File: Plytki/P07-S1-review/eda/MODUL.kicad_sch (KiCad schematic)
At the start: 23 parts, among them J5 J_MOD, U16 74AHCT125D, U17 74LVC2G17

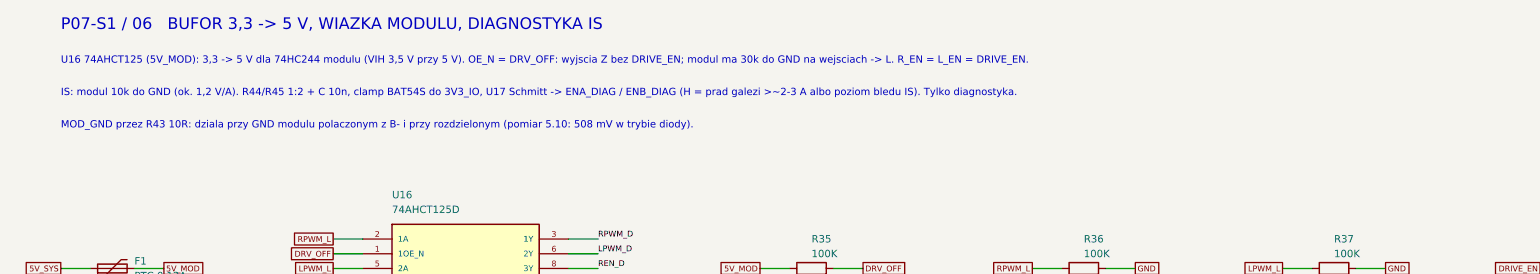
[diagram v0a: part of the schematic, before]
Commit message: P07 S1: decyzje użytkownika 5.10 w schemacie — KPWR G2RL-1-E DC5 z 5V_SYS (Q1 AO3400A, clamp do 5V_SYS, C9), J5 IDC 2x4 1:1 i wiązka W5 w BOM, F1 7,5 A, ENA/ENB_DIAG; kontrole 16/16 (mutacje 22/22), S1 30/30
Co-Authored-By: Claude Opus 5.5 <noreply@anthropic.com>
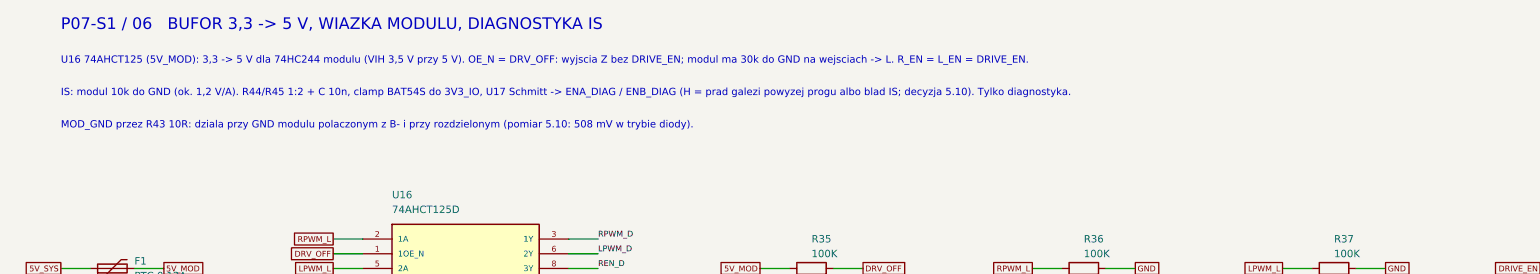
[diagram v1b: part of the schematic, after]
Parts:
- J5: MPN IDC header 2x4 2.54 mm angled shrouded, Au -> IDC box header 2x4 2.54 mm angled shrouded, Au
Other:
- note added: "IS: modul 10k do GND (ok. 1,2 V/A). R44/R45 1:2 + C 10n, clamp BAT54S do 3V3_IO, U17 Schmitt -> ENA_DIAG / ENB_DIAG (H = prad galezi powyzej progu albo blad IS; decyzja 5.10). Tylko diagnostyka."
- note removed: "IS: modul 10k do GND (ok. 1,2 V/A). R44/R45 1:2 + C 10n, clamp BAT54S do 3V3_IO, U17 Schmitt -> ENA_DIAG / ENB_DIAG (H = prad galezi >~2-3 A albo poziom bledu IS). Tylko diagnostyka."

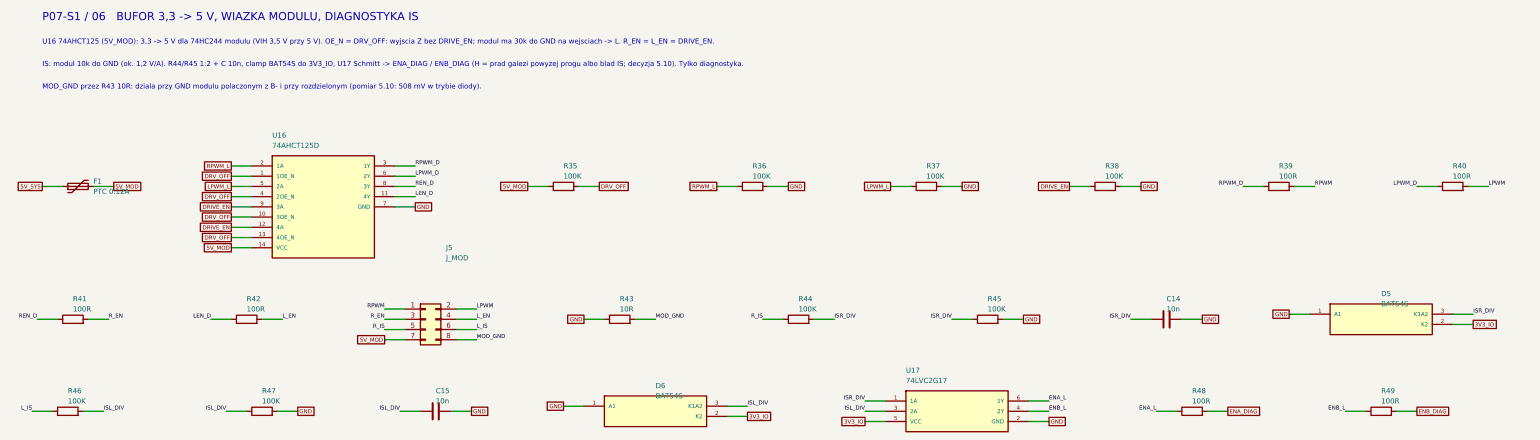
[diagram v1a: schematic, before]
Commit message: P07 S1: uproszczenia 6.10 (jedna listwa serwisowa, MOTOR_PERMIT / PWM_OUT bez odbiornika Ioff, diagnostyka IS bez Schmitta, rozmieszczenie przy złączach) — ERC 0, 16/16, S1 27/27; trasowanie nadal NIEDOMKNIĘTE (13 przerw sygnałowych), stan w README
Co-Authored-By: Claude Opus 5.5 <noreply@anthropic.com>
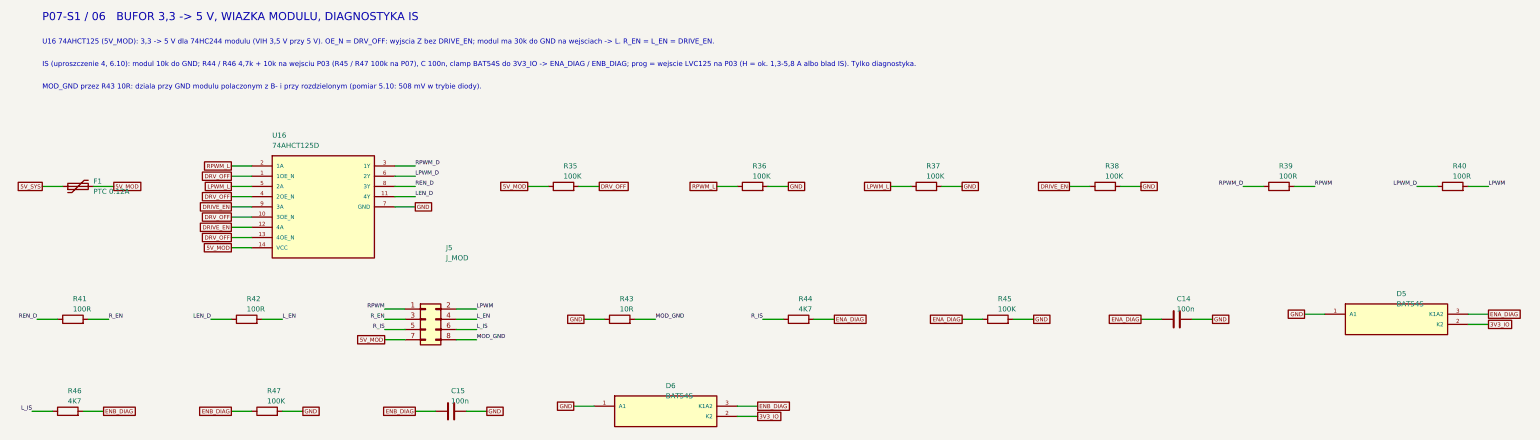
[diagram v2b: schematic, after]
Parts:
- removed R48, R49: 100R, Resistor_SMD:R_1206_3216Metric_Pad1.30x1.75mm_HandSolder, symbol P07:R
- removed U17: 74LVC2G17, Package_TO_SOT_SMD:SOT-23-6, symbol P07:74LVC2G17_SOT23_6
- C14, C15: value 10n -> 100n; MPN SMD 1206 C0G 50V 5% 10n -> SMD 1206 X7R 50V 10% 100n
- R44, R46: value 100K -> 4K7; MPN RC1206FR-07100KL -> RC1206FR-074K7L
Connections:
- net ISL_DIV is gone; now on net ENB_DIAG: C15.1, D6.3 (K1A2), R46.2, R47.1
- net ISR_DIV is gone; now on net ENA_DIAG: C14.1, D5.3 (K1A2), R44.2, R45.1
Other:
- note added: "IS (uproszczenie 4, 6.10): modul 10k do GND; R44 / R46 4,7k + 10k na wejsciu P03 (R45 / R47 100k na P07), C 100n, clamp BAT54S do 3V3_IO -> ENA_DIAG / ENB_DIAG; prog = wejscie LVC125 na P03 (H = ok. 1,3-5,8 A albo blad IS). Tylko diagnostyka."
- note removed: "IS: modul 10k do GND (ok. 1,2 V/A). R44/R45 1:2 + C 10n, clamp BAT54S do 3V3_IO, U17 Schmitt -> ENA_DIAG / ENB_DIAG (H = prad galezi powyzej progu albo blad IS; decyzja 5.10). Tylko diagnostyka."
- moved on the sheet: C14, C15, D5, D6, R45, R47
